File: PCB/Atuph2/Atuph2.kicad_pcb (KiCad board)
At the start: 2 copper layers, 153 x 120 mm, 12 parts, among them J1 Conn_01x15_Female, J2 Conn_01x15_Female

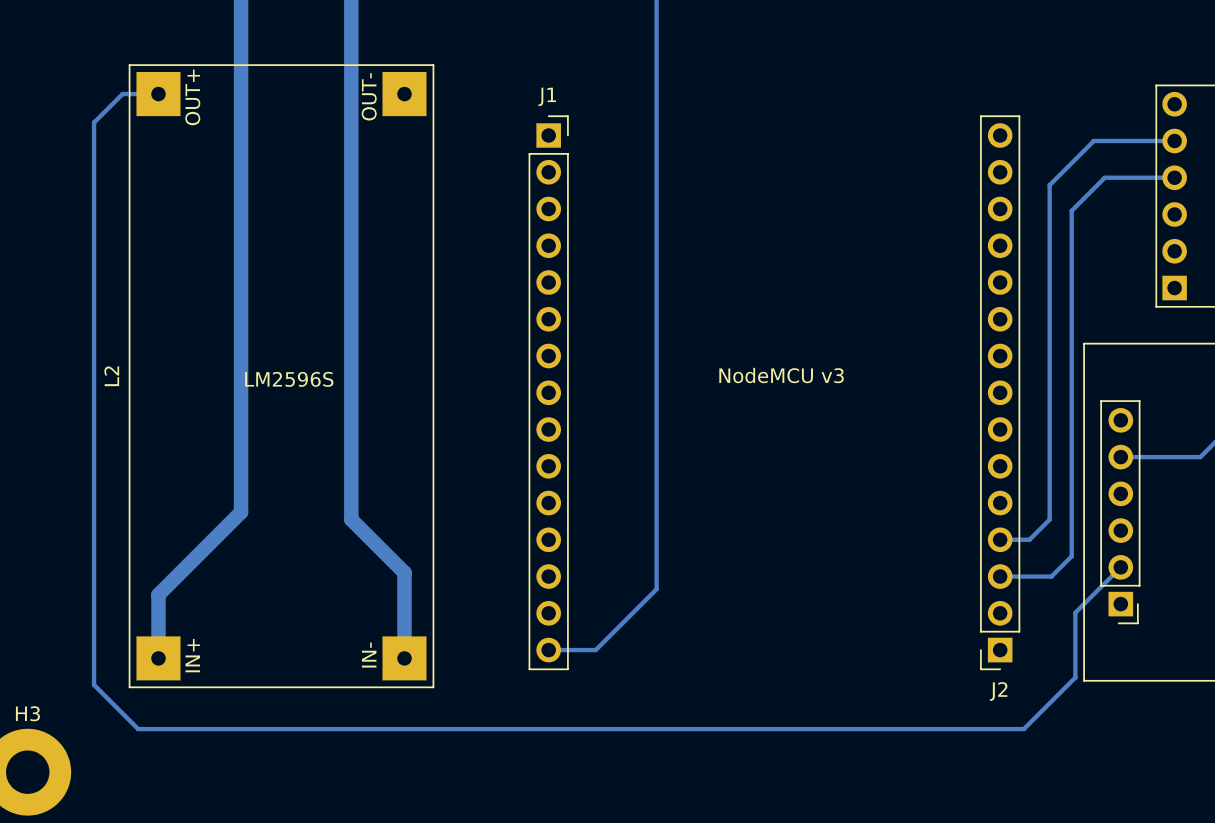
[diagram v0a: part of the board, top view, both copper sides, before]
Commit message: change PCB trace width
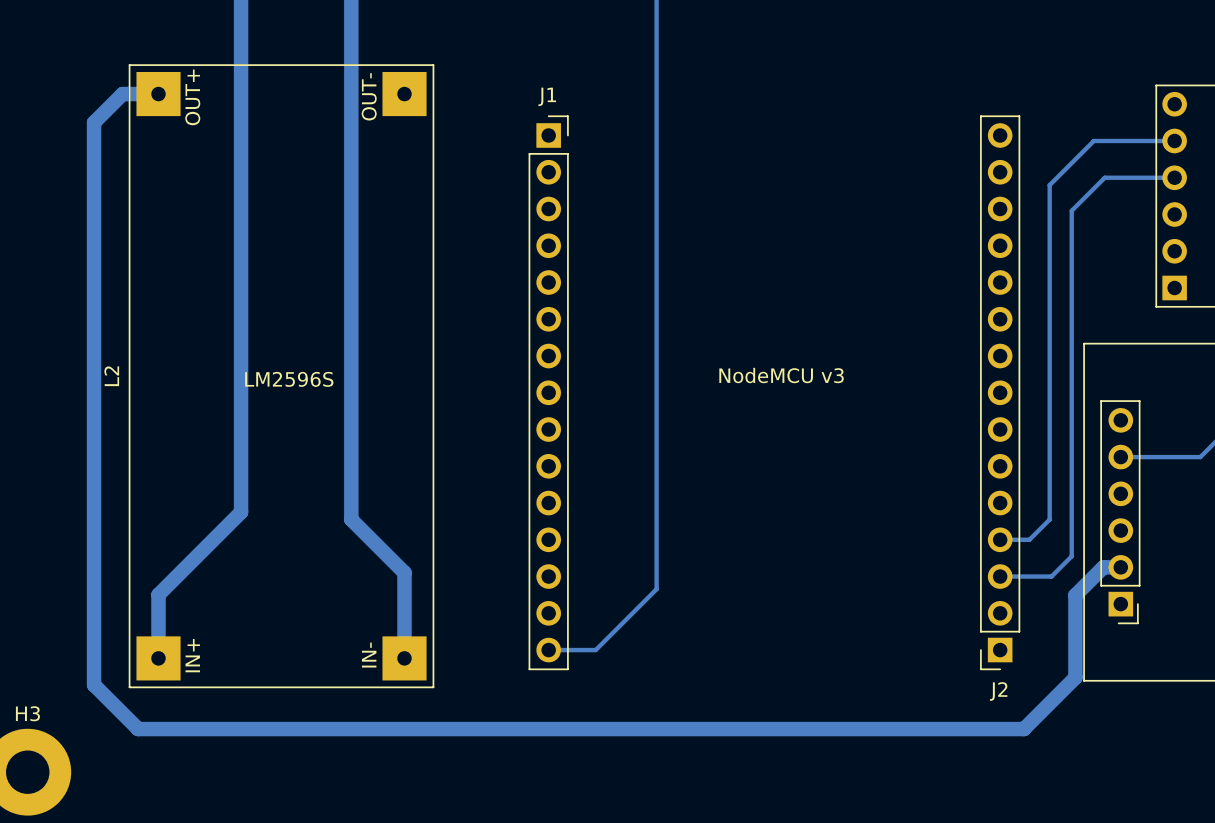
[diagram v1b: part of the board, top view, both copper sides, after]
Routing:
- net +4V: track 123.6 -> 124.3 mm

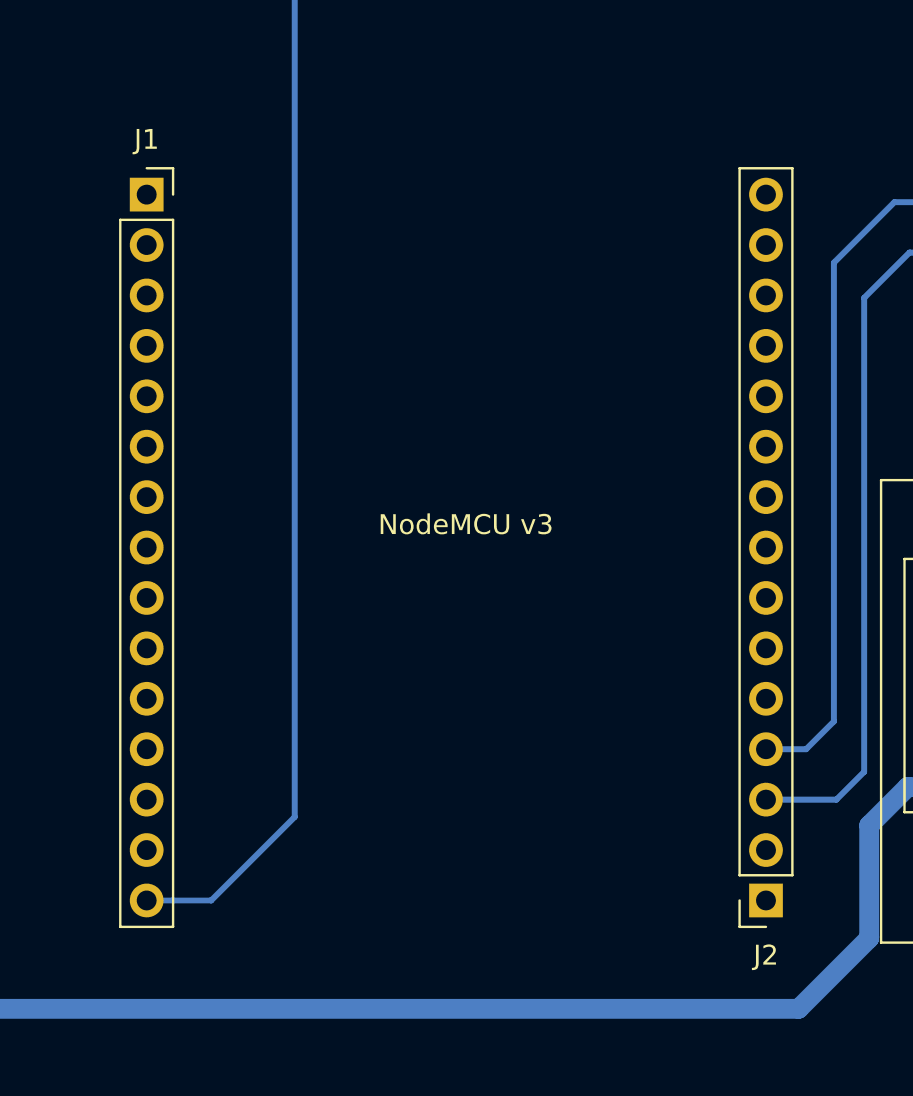
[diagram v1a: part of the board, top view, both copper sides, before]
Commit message: change nodeMCU in layout v2 to amica
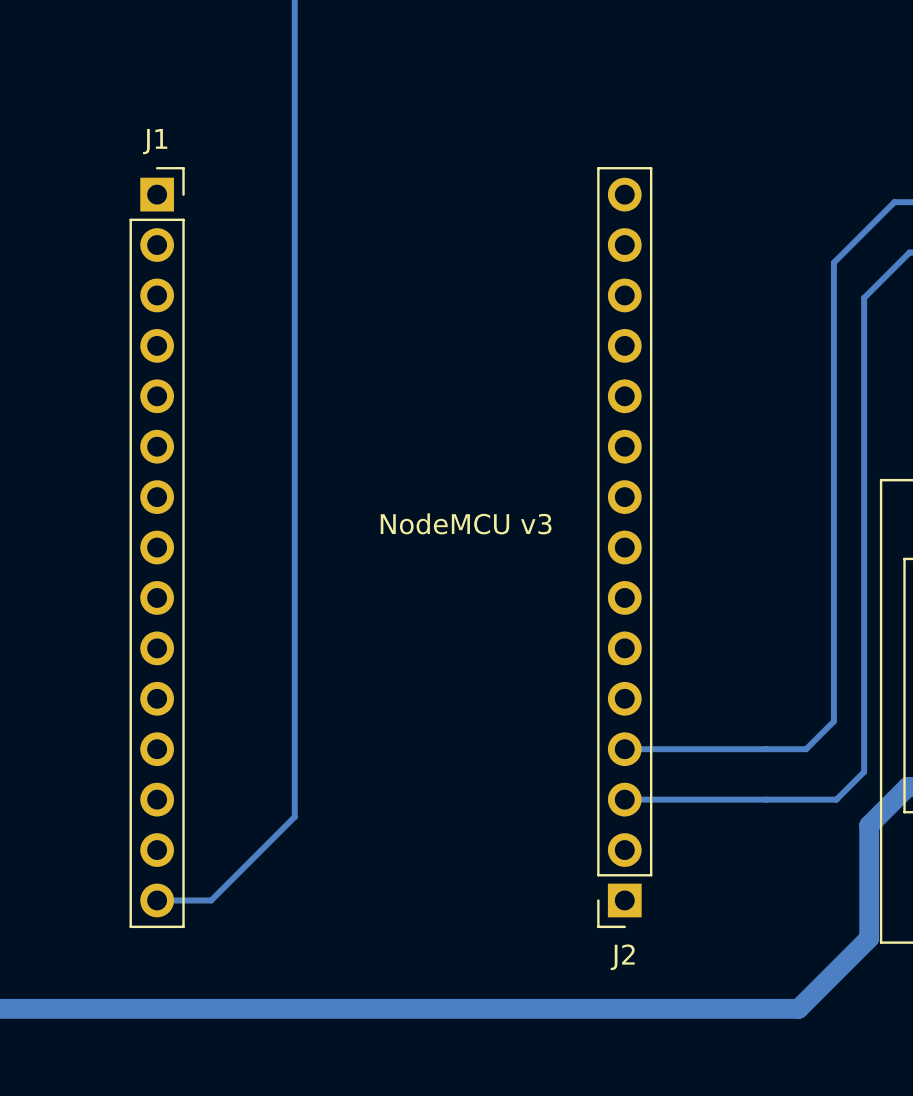
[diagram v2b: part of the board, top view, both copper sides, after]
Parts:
- moved J2 7.11 mm to (122.6, 139.6)
- moved J1 0.53 mm to (99.0, 104.0)
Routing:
- net Net-(J2-Pad4): track 37.0 -> 44.1 mm
- net Net-(J2-Pad3): track 37.5 -> 44.6 mm
- net +3V3: track 58.7 -> 58.2 mm

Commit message: add track
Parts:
- moved J1 1.00 mm to (98.0, 104.0)
- moved J2 1.00 mm to (121.6, 139.6)
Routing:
- net Net-(L1-Pad6): track 0.00 -> 38.7 mm
- net Net-(J2-Pad4): track 44.1 -> 50.9 mm
- net Net-(J2-Pad3): track 44.6 -> 48.6 mm
- net +3V3: track 58.2 -> 58.7 mm
